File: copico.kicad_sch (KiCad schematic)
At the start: 30 parts, among them P1 CocoEdgeConnector, P10 Power Bus, P2 5V Data Bus, P3 3.3V Data Bus, P4 5V Address Bus, P5 3.3V Address Bus, U1 74LS133, U2 74LS06, U3 PicoW, U4 SN74LVC245A, U5 SN74LVC245A, U6 SN74LVC245A, U7 SN74LVC4245A, U8 SN74LVC245A

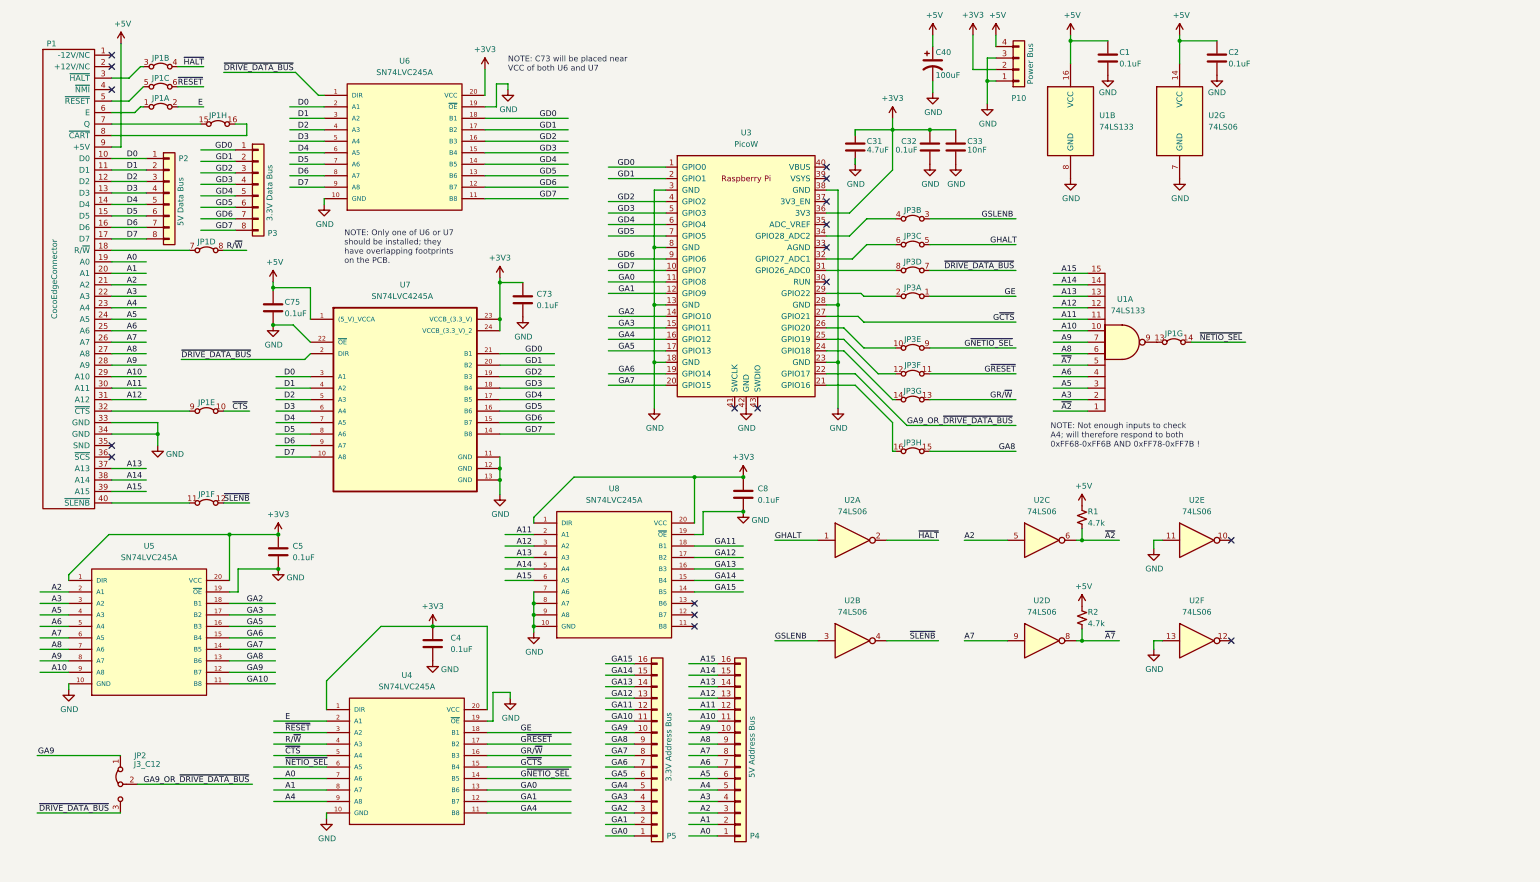
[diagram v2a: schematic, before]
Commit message: Update schematic to REV 2
The REV 2 design:

- allows the CoCo to power the PicoW via a Schottky diode, which prevents
  backfeeding one power supply from the other

- moves the address decode for the NETIO feature out of the PicoW firmware into
  discrete 74LS logic in order to allow it to respond using only PIO and DMA
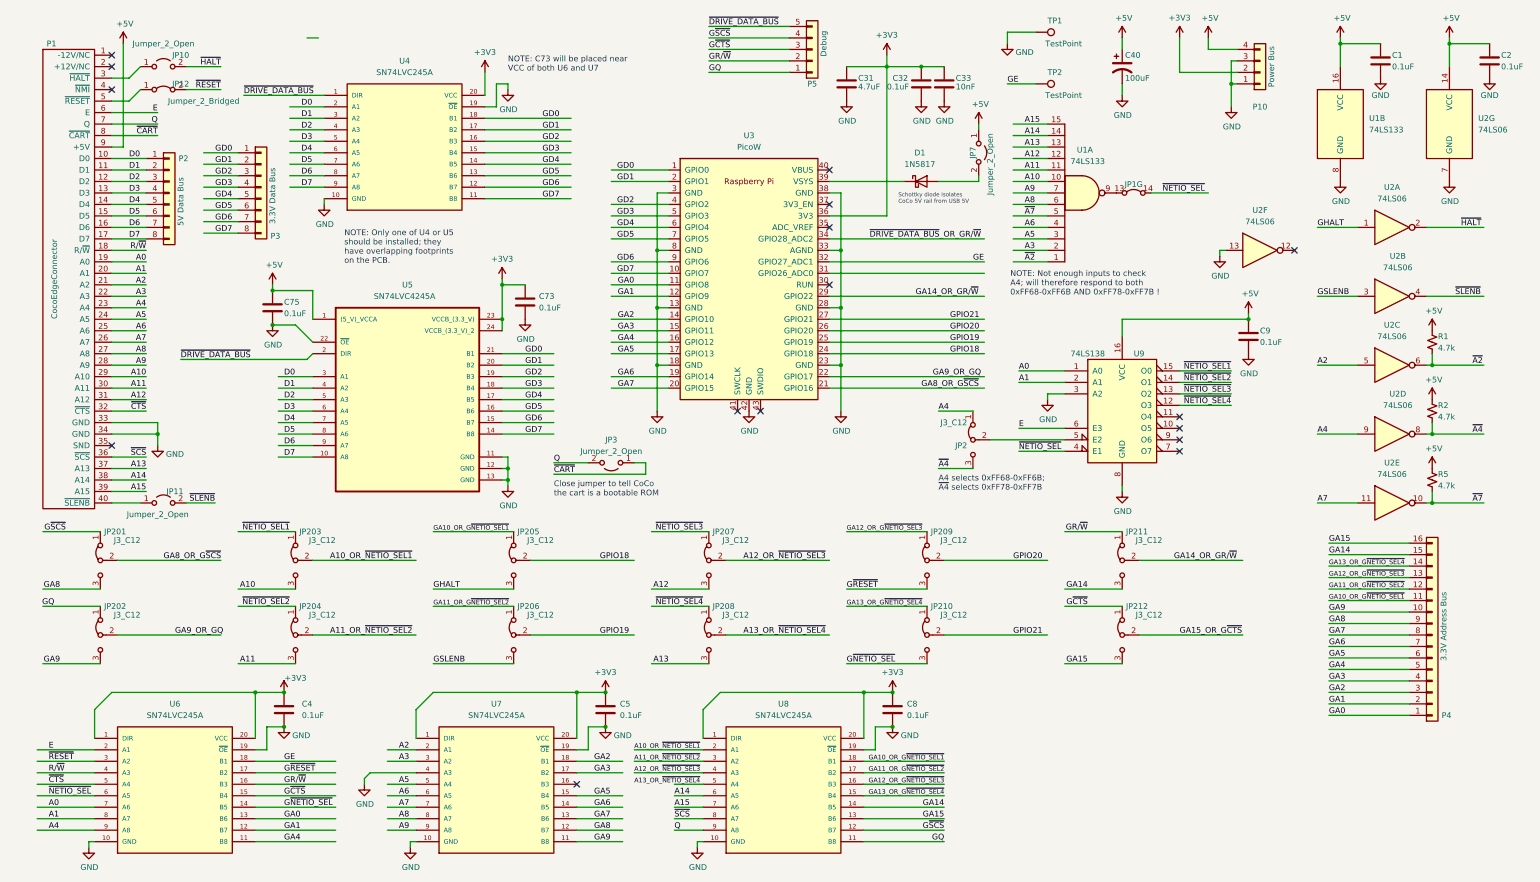
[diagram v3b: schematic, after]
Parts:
- removed unit 1 of JP1
- removed unit 4 of JP1
- removed unit 2 of JP1
- removed unit 6 of JP1
- removed unit 8 of JP1
- removed unit 5 of JP1
- removed unit 3 of JP1
- removed JP3: 8JP2NC, Connector_PinHeader_2.54mm:PinHeader_2x08_P2.54mm_Vertical, symbol Octal_Jumper_2_Bridged:Octal_Jumper_2_Bridged
- removed P5: 3.3V Address Bus, Connector_PinHeader_2.54mm:PinHeader_1x16_P2.54mm_Vertical, symbol Connector_Generic:Conn_01x16
- added C9: 0.1uF, Capacitor_THT:C_Disc_D5.0mm_W2.5mm_P5.00mm, symbol Device:C
- added D1: 1N5817, Diode_THT:D_DO-41_SOD81_P10.16mm_Horizontal, symbol Diode:1N5817
- added JP10, JP11, JP3, JP7: Jumper_2_Open, symbol Jumper:Jumper_2_Open
- added JP12: Jumper_2_Bridged, symbol Jumper:Jumper_2_Bridged
- added JP201, JP202, JP203, JP204, JP205, JP206, JP207, JP208, JP209, JP210, JP211, JP212: J3_C12, Connector_PinHeader_2.54mm:PinHeader_1x03_P2.54mm_Vertical, symbol Jumper:Jumper_3_Bridged12
- added P5: Debug, Connector_PinHeader_2.54mm:PinHeader_1x04_P2.54mm_Vertical, symbol Connector_Generic:Conn_01x05
- added R5: 4.7k, Resistor_THT:R_Axial_DIN0207_L6.3mm_D2.5mm_P10.16mm_Horizontal, symbol Device:R_Small_US
- added TP1, TP2: TestPoint, symbol Connector:TestPoint
- added U9: 74LS138, symbol 74xx:74LS138
- P4: value 5V Address Bus -> 3.3V Address Bus
- U5: renamed from U7; footprint 00_Custom:MDFLY_MOL-CV0089_SN74LVC4245A -> Package_SO:SOIC-24W_7.5x15.4mm_P1.27mm
- renumbered U6 to U4, U4 to U6, U5 to U7
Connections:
- net GA10 is gone; now on net GA9: U7.11 (B8)
- net +5V: now also C9.1, JP7.1 (A), R5.1, U9.16 (VCC)
- net A0: now also U9.1 (A0); no longer P4.1 (Pin_1)
- net A1: now also U9.2 (A1); no longer P4.2 (Pin_2)
- net A10: now also JP203.3 (B); no longer P4.11 (Pin_11), U7.9 (A8)
- net A11: now also JP204.3 (B); no longer P4.12 (Pin_12), U8.2 (A1)
- net A12: now also JP207.3 (B); no longer P4.13 (Pin_13), U8.3 (A2)
- net A13: now also JP208.3 (B); no longer P4.14 (Pin_14), U8.4 (A3)
- net A14: now also U8.6 (A5); no longer P4.15 (Pin_15), U8.5 (A4)
- net A15: now also U8.7 (A6); no longer P4.16 (Pin_16), U8.6 (A5)
- net A2: no longer P4.3 (Pin_3)
- net A3: no longer P4.4 (Pin_4)
- net A4: now also JP2.1 (A), U2.9; no longer P4.5 (Pin_5)
- net A5: now also U7.5 (A4); no longer P4.6 (Pin_6), U7.4 (A3)
- net A6: now also U7.6 (A5); no longer P4.7 (Pin_7), U7.5 (A4)
- net A7: now also U2.11, U7.7 (A6); no longer P4.8 (Pin_8), U2.9, U7.6 (A5)
- net A8: now also U7.8 (A7); no longer P4.9 (Pin_9), U7.7 (A6)
- net A9: now also U7.9 (A8); no longer P4.10 (Pin_10), U7.8 (A7)
- net E: now also P1.6 (E), U9.6 (E3)
- net GA0: now also P4.1 (Pin_1)
- net GA1: now also P4.2 (Pin_2)
- net GA14: now also P4.15 (Pin_15), U8.14 (B5), JP211.3 (B); no longer U8.15 (B4)
- net GA15: now also P4.16 (Pin_16), U8.13 (B6), JP212.3 (B); no longer U8.14 (B5)
- net GA2: now also P4.3 (Pin_3)
- net GA3: now also P4.4 (Pin_4)
- net GA4: now also P4.5 (Pin_5)
- net GA5: now also P4.6 (Pin_6), U7.15 (B4); no longer U7.16 (B3)
- net GA6: now also P4.7 (Pin_7), U7.14 (B5); no longer U7.15 (B4)
- net GA7: now also P4.8 (Pin_8), U7.13 (B6); no longer U7.14 (B5)
- net GA8: now also P4.9 (Pin_9), U7.12 (B7), JP201.3 (B); no longer U7.13 (B6)
- net GA9: now also P4.10 (Pin_10), JP202.3 (B); no longer JP2.1 (A), U7.12 (B7)
- net GE: now also U3.32 (GPIO27_ADC1), TP2.1
- net GHALT: now also JP205.3 (B)
- net GND: now also U3.33 (AGND), U7.4 (A3), C9.2, TP1.1, U9.3 (A2), U9.8 (GND); no longer U2.11, U8.7 (A6), U8.8 (A7), U8.9 (A8)
- net GR/~{W}: now also JP211.1 (A), P5.2 (Pin_2)
- net GSLENB: now also JP206.3 (B)
- net G~{CTS}: now also JP212.1 (A), P5.3 (Pin_3); no longer U3.27 (GPIO21)
- net G~{NETIO_SEL}: now also JP210.3 (B)
- net G~{RESET}: now also JP209.3 (B)
- net R/~{W}: now also P1.18 (R/~{W})
- net ~{A7}: now also U2.10, R5.2; no longer R2.2, U2.8
- net ~{CTS}: now also P1.32 (~{CTS})
- net ~{DRIVE_DATA_BUS}: now also P5.5 (Pin_5); no longer JP2.3 (B)
- net ~{HALT}: now also JP10.2 (B)
- net ~{NETIO_SEL}: now also U9.4 (E1)
- net ~{RESET}: now also JP12.2 (B)
- net ~{SLENB}: now also JP11.2 (B)
- net at P1.3 (~{HALT}): now also JP10.1 (A)
- net ~{SCS}: now reaches P1.36 (~{SCS})
- net ~{SCS}: now also U8.8 (A7)
- net at P1.40 (~{SLENB}): now also JP11.1 (A)
- net at P1.5 (~{RESET}): now also JP12.1 (A)
- net Q: now reaches P1.7 (Q)
- net Q: now also U8.9 (A8), JP3.2 (B)
- net ~{CART}: now reaches P1.8 (~{CART})
- net ~{CART}: now also JP3.1 (A)
- net GPIO19: now reaches U3.25 (GPIO19)
- net GPIO19: now also JP206.2 (C)
- net GA8_OR_G~{SCS}: now reaches U3.21 (GPIO16)
- net GA8_OR_G~{SCS}: now also JP201.2 (C)
- net GA14_OR_GR/~{W}: now reaches U3.29 (GPIO22)
- net GA14_OR_GR/~{W}: now also JP211.2 (C)
- net GPIO18: now reaches U3.24 (GPIO18)
- net GPIO18: now also JP205.2 (C)
- net GQ: now reaches U8.11 (B8)
- net GQ: now also JP202.1 (A), P5.1 (Pin_1)
- net G~{SCS}: now reaches U8.12 (B7)
- net G~{SCS}: now also JP201.1 (A), P5.4 (Pin_4)
- net ~{DRIVE_DATA_BUS}_OR_GR/~{W}: now reaches U3.34 (GPIO28_ADC2)
- net GPIO20: now reaches U3.26 (GPIO20)
- net GPIO20: now also JP209.2 (C)
- net at U3.39 (VSYS): now also D1.1 (K)
- net GA11 renamed GA10_OR_G~{NETIO_SEL1}
- net GA10_OR_G~{NETIO_SEL1}: now also P4.11 (Pin_11), JP205.1 (A)
- net GA12 renamed GA11_OR_G~{NETIO_SEL2}
- net GA11_OR_G~{NETIO_SEL2}: now also P4.12 (Pin_12), JP206.1 (A)
- net GA13 renamed GA12_OR_G~{NETIO_SEL3}
- net GA12_OR_G~{NETIO_SEL3}: now also P4.13 (Pin_13), JP209.1 (A)
- net GA9_OR_~{DRIVE_DATA_BUS}: no longer names the net of JP2.2 (C)
- net GA9_OR_~{DRIVE_DATA_BUS}: now also U9.5 (E2); no longer U3.22 (GPIO17)
- new net: D1.2 (A), JP7.2 (B)
- new net A10_OR_~{NETIO_SEL1}: JP203.2 (C), U8.2 (A1)
- new net A11_OR_~{NETIO_SEL2}: JP204.2 (C), U8.3 (A2)
- new net A12_OR_~{NETIO_SEL3}: JP207.2 (C), U8.4 (A3)
- new net A13_OR_~{NETIO_SEL4}: JP208.2 (C)
- new net GA13_OR_G~{NETIO_SEL4}: JP210.1 (A), P4.14 (Pin_14), U8.15 (B4)
- new net GA15_OR_G~{CTS}: JP212.2 (C)
- new net GA9_OR_GQ: JP202.2 (C), U3.22 (GPIO17)
- new net GPIO21: JP210.2 (C), U3.27 (GPIO21)
- new net ~{A4}: JP2.3 (B), R2.2, U2.8
- new net ~{NETIO_SEL1}: JP203.1 (A), U9.15 (O0)
- new net ~{NETIO_SEL2}: JP204.1 (A), U9.14 (O1)
- new net ~{NETIO_SEL3}: JP207.1 (A), U9.13 (O2)
- new net ~{NETIO_SEL4}: JP208.1 (A), U9.12 (O3)
- no-connect marks 18 -> 16
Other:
- note added: "A4 selects 0xFF68-0xFF6B; ~{A4} selects 0xFF78-0xFF7B"
- note added: "Close jumper to tell CoCo the cart is a bootable ROM"
- note added: "NOTE: Only one of U4 or U5 should be installed; they have overlapping footprints on the PCB."
- note added: "Schottky diode isolates CoCo 5V rail from USB 5V"
- note removed: "NOTE: Only one of U6 or U7 should be installed; they have overlapping footprints on the PCB."
- moved on the sheet: C1, C2, C31, C32, C33, C4, C40, C5, C73, C8, JP1G, P10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

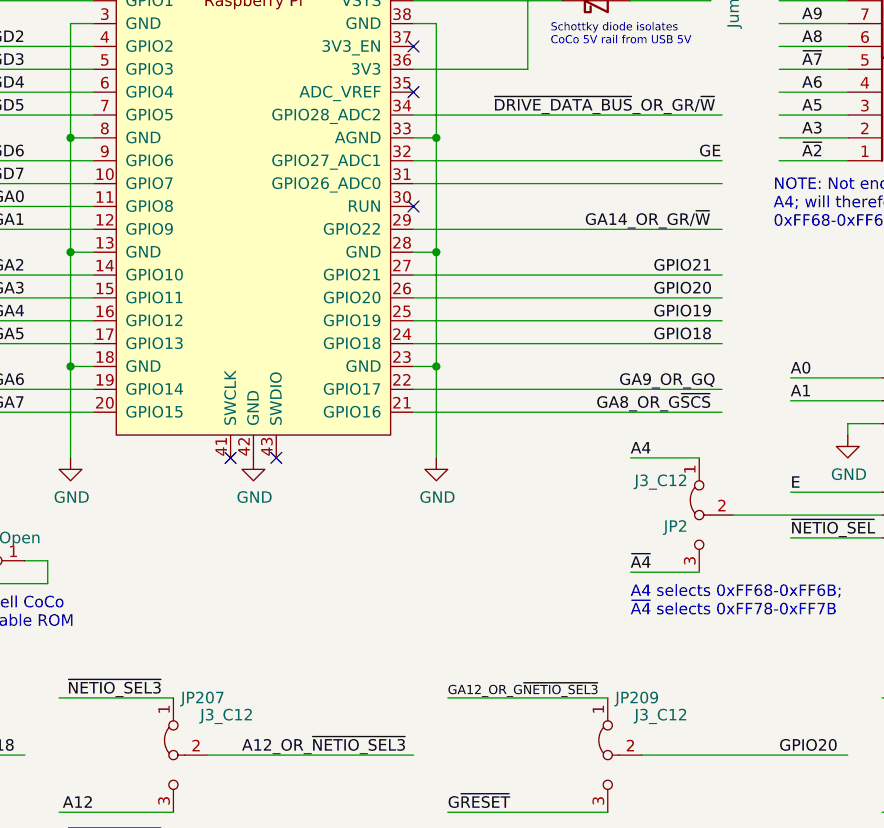
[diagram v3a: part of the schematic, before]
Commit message: FIXME: need pull-up R when DRIVE_DATA_BUS floating
Add a FIXME that indicates the need for DRIVE_DATA_BUS to be pulled high when
the GPIO28 jumper is set to send GR//W to the PicoW instead of getting
DRIVE_DATA_BUS from the PicoW on that GPIO
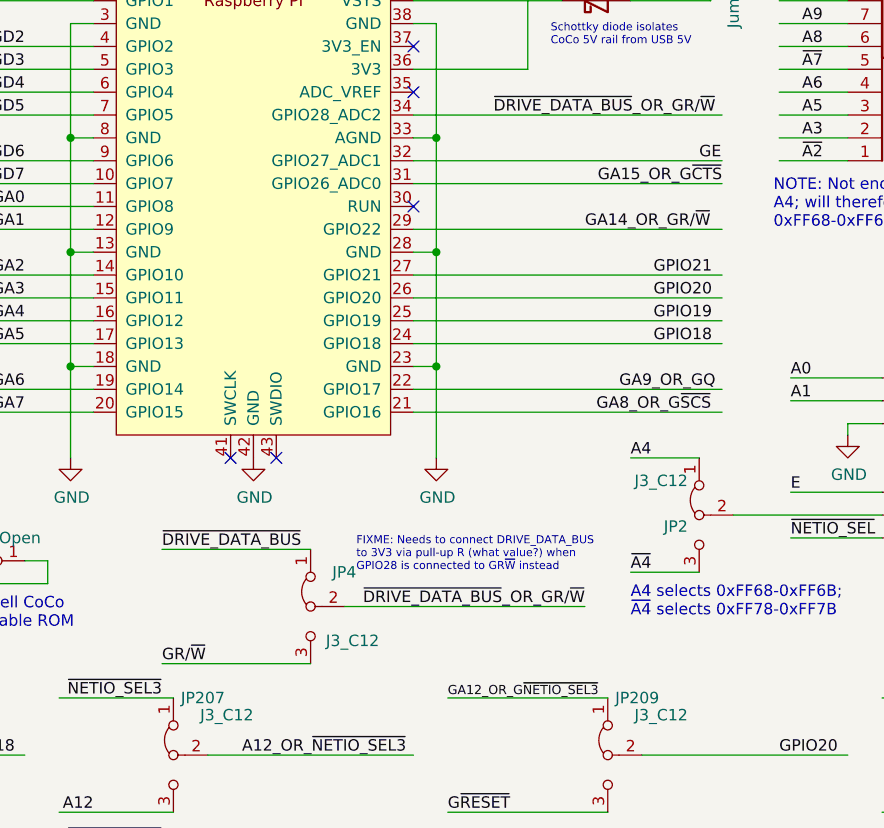
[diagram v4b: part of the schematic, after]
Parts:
- added JP4: J3_C12, Connector_PinHeader_2.54mm:PinHeader_1x03_P2.54mm_Vertical, symbol Jumper:Jumper_3_Bridged12
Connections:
- net GA15_OR_G~{CTS}: now also U3.31 (GPIO26_ADC0)
- net GR/~{W}: now also JP4.3 (B)
- net ~{DRIVE_DATA_BUS}: now also JP4.1 (A)
- net ~{DRIVE_DATA_BUS}_OR_GR/~{W}: now also JP4.2 (C)
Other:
- note added: "FIXME: Needs to connect DRIVE_DATA_BUS to 3V3 via pull-up R (what value?) when GPIO28 is connected to GR~{W} instead"
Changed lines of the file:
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@@
   (title_block
     (title "CoPiCo: WiFi and more for the Tandy Color Computer")
-    (date "2024-04-17")
-    (rev "0.2.5")
+    (date "2024-04-18")
+    (rev "0.2.6")
     (company "Thomas Shanks (copico@tshanks.org)")
     (comment 1 "found at: github.com/JayesonLS/TandyCircuitsAndLogic/tree/master/CoCoProtoBoard")
@@
     (stroke (width 0) (type default))
   )
+  (wire (pts (xy 161.29 124.46) (xy 177.8 124.46))
+    (stroke (width 0) (type default))
+  )
   (wire (pts (xy 196.85 196.85) (xy 214.63 196.85))
     (stroke (width 0) (type default))
@@
     (stroke (width 0) (type default))
   )
+  (wire (pts (xy 181.61 118.11) (xy 208.28 118.11))
+    (stroke (width 0) (type default))
+  )
   (wire (pts (xy 67.31 104.14) (xy 74.93 104.14))
     (stroke (width 0) (type default))
@@
     (stroke (width 0) (type default))
   )
+  (wire (pts (xy 161.29 111.76) (xy 177.8 111.76))
+    (stroke (width 0) (type default))
+  )
   (wire (pts (xy 30.48 35.56) (xy 40.64 35.56))
     (stroke (width 0) (type default))
@@
     (effects (font (size 1.27 1.27)) (justify left bottom))
   )
+  (text "FIXME: Needs to connect DRIVE_DATA_BUS\nto 3V3 via pull-up R (what value?) when\nGPIO28 is connected to GR~{W} instead"
+    (at 182.88 114.3 0)
+    (effects (font (size 0.889 0.889)) (justify left bottom))
+  )
   (text "A4 selects 0xFF68-0xFF6B;\n~{A4} selects 0xFF78-0xFF7B"
     (at 213.36 119.38 0)
@@
     (effects (font (size 1.27 1.27)) (justify left bottom))
   )
+  (label "~{DRIVE_DATA_BUS}" (at 161.29 111.76 0) (fields_autoplaced)
+    (effects (font (size 1.27 1.27)) (justify left bottom))
+  )
   (label "~{A4}" (at 331.47 106.68 0) (fields_autoplaced)
     (effects (font (size 1.27 1.27)) (justify left bottom))
@@
     (effects (font (size 1.27 1.27)) (justify left bottom))
   )
+  (label "~{DRIVE_DATA_BUS}_OR_GR{slash}~{W}" (at 208.28 118.11 180) (fields_autoplaced)
+    (effects (font (size 1.27 1.27)) (justify right bottom))
+  )
   (label "GA15_OR_G~{CTS}" (at 266.7 151.13 0) (fields_autoplaced)
     (effects (font (size 1.27 1.27)) (justify left bottom))
@@
     (effects (font (size 1.27 1.27)) (justify left bottom))
   )
+  (label "GA15_OR_G~{CTS}" (at 223.52 71.12 180) (fields_autoplaced)
+    (effects (font (size 1.27 1.27)) (justify right bottom))
+  )
   (label "G~{RESET}" (at 193.04 140.97 0) (fields_autoplaced)
     (effects (font (size 1.27 1.27)) (justify left bottom))
@@
     (effects (font (size 1.27 1.27)) (justify right bottom))
   )
+  (label "GR{slash}~{W}" (at 161.29 124.46 0) (fields_autoplaced)
+    (effects (font (size 1.27 1.27)) (justify left bottom))
+  )
   (label "GA5" (at 137.16 186.69 0) (fields_autoplaced)
     (effects (font (size 1.27 1.27)) (justify left bottom))
@@
         )
       )
+    )
+  )
+  (symbol (lib_id "Jumper:Jumper_3_Bridged12") (at 177.8 118.11 90) (mirror x) (unit 1)
+    (in_bom yes) (on_board yes) (dnp no)
+    (property "Reference" "JP4" (at 182.88 114.3 90)
+      (effects (font (size 1.27 1.27)) (justify left))
+    )
+    (property "Value" "J3_C12" (at 185.42 121.92 90)
+      (effects (font (size 1.27 1.27)) (justify left))
+    )
+    (property "Footprint" "Connector_PinHeader_2.54mm:PinHeader_1x03_P2.54mm_Vertical" (at 177.8 118.11 0)
+      (effects (font (size 1.27 1.27)) hide)
+    )
+    (property "Datasheet" "~" (at 177.8 118.11 0)
+      (effects (font (size 1.27 1.27)) hide)
+    )
+    (pin "3")
+    (pin "2")
+    (pin "1")
+    (instances
+      (project "copico"
+        (path "/50d84e83-af39-4327-b4b6-a5a8c6074de2"
+          (reference "JP4") (unit 1)
+        )
+      )
